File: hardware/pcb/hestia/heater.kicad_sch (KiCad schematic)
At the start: 19 parts, among them Q1 FDS8876, SW2 SW_Push_Open, U10 INA826

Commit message: changes
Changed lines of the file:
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@@
     (effects (font (size 1.27 1.27)) (justify left bottom))
   )
-  (label "Heater low" (at 135.89 103.505 0)
+  (label "Heater low" (at 136.525 103.505 0)
     (effects (font (size 1.27 1.27)) (justify left bottom))
   )

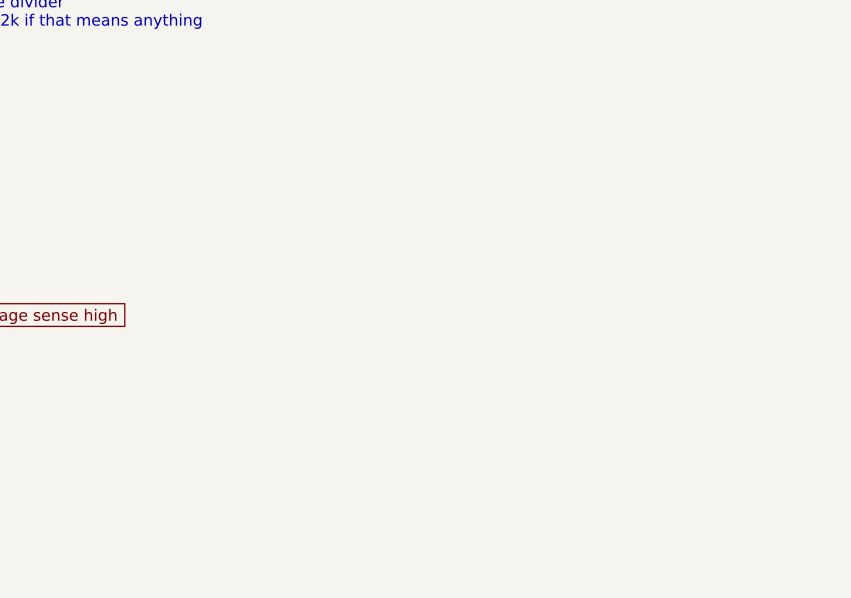
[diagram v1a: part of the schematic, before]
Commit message: pcb: lots of schematic cleanup, board not yet updated
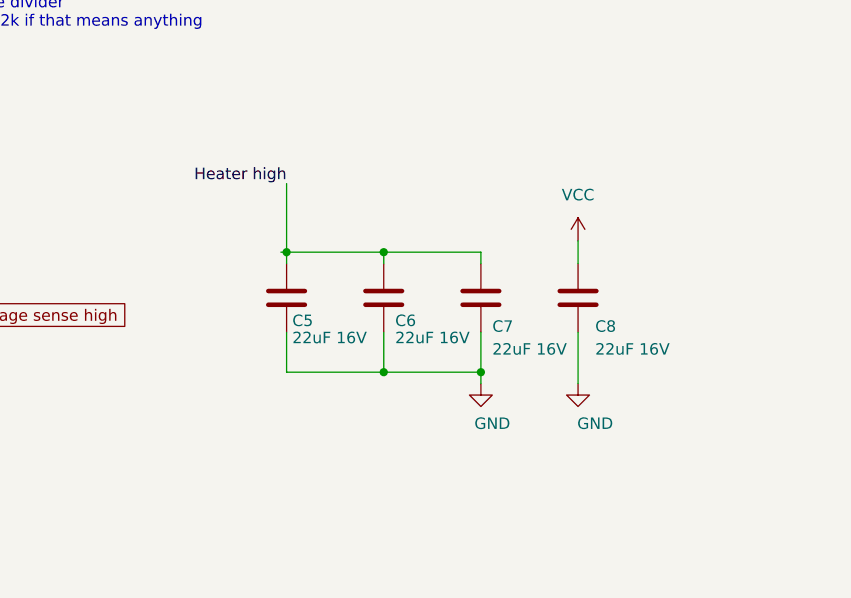
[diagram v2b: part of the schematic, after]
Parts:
- added C5, C6, C7, C8: 22uF 16V, Capacitor_SMD:C_1206_3216Metric, symbol Device:C
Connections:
- net GND: now also C5.2, C6.2, C7.2, C8.2
- net Heater high: now also C5.1, C6.1, C7.1
- net VCC: now also C8.1
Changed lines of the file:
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@@
   (junction (at 103.505 56.515) (diameter 0) (color 0 0 0 0)
   )
+  (junction (at 228.6 72.39) (diameter 0) (color 0 0 0 0)
+  )
   (junction (at 88.265 74.295) (diameter 0) (color 0 0 0 0)
   )
   (junction (at 112.395 122.555) (diameter 0) (color 0 0 0 0)
   )
+  (junction (at 217.805 59.055) (diameter 0) (color 0 0 0 0)
+  )
   (junction (at 83.185 60.96) (diameter 0) (color 0 0 0 0)
   )
+  (junction (at 217.805 72.39) (diameter 0) (color 0 0 0 0)
+  )
   (junction (at 129.54 131.445) (diameter 0) (color 0 0 0 0)
   )
@@
   (junction (at 81.915 51.435) (diameter 0) (color 0 0 0 0)
   )
+  (junction (at 207.01 59.055) (diameter 0) (color 0 0 0 0)
+  )
   (junction (at 129.54 89.535) (diameter 0) (color 0 0 0 0)
   )
+  (wire (pts (xy 207.01 72.39) (xy 217.805 72.39))
+    (stroke (width 0) (type default) (color 0 0 0 0))
+  )
   (wire (pts (xy 88.265 79.375) (xy 88.265 81.915))
     (stroke (width 0) (type default) (color 0 0 0 0))
@@
     (stroke (width 0) (type default) (color 0 0 0 0))
   )
+  (wire (pts (xy 207.01 59.055) (xy 206.375 59.055))
+    (stroke (width 0) (type default) (color 0 0 0 0))
+  )
   (wire (pts (xy 81.915 51.435) (xy 103.505 51.435))
     (stroke (width 0) (type default) (color 0 0 0 0))
@@
     (stroke (width 0) (type default) (color 0 0 0 0))
   )
+  (wire (pts (xy 207.01 67.945) (xy 207.01 72.39))
+    (stroke (width 0) (type default) (color 0 0 0 0))
+  )
   (wire (pts (xy 129.54 89.535) (xy 135.89 89.535))
     (stroke (width 0) (type default) (color 0 0 0 0))
@@
     (stroke (width 0) (type default) (color 0 0 0 0))
   )
+  (wire (pts (xy 207.01 51.435) (xy 207.01 59.055))
+    (stroke (width 0) (type default) (color 0 0 0 0))
+  )
+  (wire (pts (xy 207.01 59.055) (xy 207.01 60.325))
+    (stroke (width 0) (type default) (color 0 0 0 0))
+  )
   (wire (pts (xy 103.505 64.135) (xy 103.505 56.515))
     (stroke (width 0) (type default) (color 0 0 0 0))
@@
     (stroke (width 0) (type default) (color 0 0 0 0))
   )
+  (wire (pts (xy 228.6 59.055) (xy 228.6 60.325))
+    (stroke (width 0) (type default) (color 0 0 0 0))
+  )
   (wire (pts (xy 100.965 141.605) (xy 100.965 142.875))
     (stroke (width 0) (type default) (color 0 0 0 0))
@@
     (stroke (width 0) (type default) (color 0 0 0 0))
   )
+  (wire (pts (xy 217.805 59.055) (xy 228.6 59.055))
+    (stroke (width 0) (type default) (color 0 0 0 0))
+  )
   (wire (pts (xy 127 102.235) (xy 127 104.775))
     (stroke (width 0) (type default) (color 0 0 0 0))
@@
     (stroke (width 0) (type default) (color 0 0 0 0))
   )
+  (wire (pts (xy 239.395 57.785) (xy 239.395 60.325))
+    (stroke (width 0) (type default) (color 0 0 0 0))
+  )
   (wire (pts (xy 106.045 86.995) (xy 106.045 88.265))
     (stroke (width 0) (type default) (color 0 0 0 0))
@@
     (stroke (width 0) (type default) (color 0 0 0 0))
   )
+  (wire (pts (xy 217.805 67.945) (xy 217.805 72.39))
+    (stroke (width 0) (type default) (color 0 0 0 0))
+  )
+  (wire (pts (xy 239.395 67.945) (xy 239.395 73.66))
+    (stroke (width 0) (type default) (color 0 0 0 0))
+  )
   (wire (pts (xy 129.54 131.445) (xy 129.54 133.985))
     (stroke (width 0) (type default) (color 0 0 0 0))
   )
+  (wire (pts (xy 217.805 72.39) (xy 228.6 72.39))
+    (stroke (width 0) (type default) (color 0 0 0 0))
+  )
+  (wire (pts (xy 228.6 72.39) (xy 228.6 73.66))
+    (stroke (width 0) (type default) (color 0 0 0 0))
+  )
   (wire (pts (xy 98.425 122.555) (xy 100.965 122.555))
     (stroke (width 0) (type default) (color 0 0 0 0))
@@
     (stroke (width 0) (type default) (color 0 0 0 0))
   )
+  (wire (pts (xy 217.805 60.325) (xy 217.805 59.055))
+    (stroke (width 0) (type default) (color 0 0 0 0))
+  )
   (wire (pts (xy 103.505 56.515) (xy 103.505 51.435))
     (stroke (width 0) (type default) (color 0 0 0 0))
@@
     (stroke (width 0) (type default) (color 0 0 0 0))
   )
+  (wire (pts (xy 207.01 59.055) (xy 217.805 59.055))
+    (stroke (width 0) (type default) (color 0 0 0 0))
+  )
   (wire (pts (xy 118.745 59.055) (xy 118.745 61.595))
     (stroke (width 0) (type default) (color 0 0 0 0))
   )
   (wire (pts (xy 129.54 99.06) (xy 129.54 103.505))
+    (stroke (width 0) (type default) (color 0 0 0 0))
+  )
+  (wire (pts (xy 228.6 67.945) (xy 228.6 72.39))
     (stroke (width 0) (type default) (color 0 0 0 0))
   )
@@
     (at 158.115 34.29 0)
     (effects (font (size 1.27 1.27)) (justify left bottom))
+  )
+  (label "Heater high" (at 207.01 51.435 180)
+    (effects (font (size 1.27 1.27)) (justify right bottom))
   )
   (label "Heater high" (at 163.83 54.61 90)
@@
     (pin "1")
   )
+  (symbol (lib_id "power:VCC") (at 239.395 57.785 0) (unit 1)
+    (in_bom yes) (on_board yes) (fields_autoplaced)
+    (property "Reference" "#PWR07" (id 0) (at 239.395 61.595 0)
+      (effects (font (size 1.27 1.27)) hide)
+    )
+    (property "Value" "VCC" (id 1) (at 239.395 52.705 0))
+    (property "Footprint" "" (id 2) (at 239.395 57.785 0)
+      (effects (font (size 1.27 1.27)) hide)
+    )
+    (property "Datasheet" "" (id 3) (at 239.395 57.785 0)
+      (effects (font (size 1.27 1.27)) hide)
+    )
+    (pin "1")
+  )
   (symbol (lib_id "power:VCC") (at 129.54 73.66 0) (unit 1)
     (in_bom yes) (on_board yes) (fields_autoplaced)
@@
     )
     (pin "1")
+  )
+  (symbol (lib_id "Device:C") (at 239.395 64.135 0) (unit 1)
+    (in_bom yes) (on_board yes)
+    (property "Reference" "C8" (id 0) (at 241.3 67.31 0)
+      (effects (font (size 1.27 1.27)) (justify left))
+    )
+    (property "Value" "22uF 16V" (id 1) (at 241.3 69.85 0)
+      (effects (font (size 1.27 1.27)) (justify left))
+    )
+    (property "Footprint" "Capacitor_SMD:C_1206_3216Metric" (id 2) (at 240.3602 67.945 0)
+      (effects (font (size 1.27 1.27)) hide)
+    )
+    (property "Datasheet" "~" (id 3) (at 239.395 64.135 0)
+      (effects (font (size 1.27 1.27)) hide)
+    )
+    (property "LCSC Part" "C13585" (id 4) (at 239.395 64.135 0)
+      (effects (font (size 1.27 1.27)) hide)
+    )
+    (pin "1")
+    (pin "2")
   )
   (symbol (lib_id "Device:R") (at 106.045 122.555 90) (unit 1)
@@
     (pin "2")
   )
+  (symbol (lib_id "power:GND") (at 228.6 73.66 0) (unit 1)
+    (in_bom yes) (on_board yes)
+    (property "Reference" "#PWR0173" (id 0) (at 228.6 80.01 0)
+      (effects (font (size 1.27 1.27)) hide)
+    )
+    (property "Value" "GND" (id 1) (at 229.87 78.105 0))
+    (property "Footprint" "" (id 2) (at 228.6 73.66 0)
+      (effects (font (size 1.27 1.27)) hide)
+    )
+    (property "Datasheet" "" (id 3) (at 228.6 73.66 0)
+      (effects (font (size 1.27 1.27)) hide)
+    )
+    (pin "1")
+  )
   (symbol (lib_id "Device:R") (at 163.195 103.505 180) (unit 1)
     (in_bom yes) (on_board yes) (fields_autoplaced)
@@
     (pin "2")
   )
+  (symbol (lib_id "Device:C") (at 217.805 64.135 0) (unit 1)
+    (in_bom yes) (on_board yes)
+    (property "Reference" "C6" (id 0) (at 219.075 66.675 0)
+      (effects (font (size 1.27 1.27)) (justify left))
+    )
+    (property "Value" "22uF 16V" (id 1) (at 219.075 68.58 0)
+      (effects (font (size 1.27 1.27)) (justify left))
+    )
+    (property "Footprint" "Capacitor_SMD:C_1206_3216Metric" (id 2) (at 218.7702 67.945 0)
+      (effects (font (size 1.27 1.27)) hide)
+    )
+    (property "Datasheet" "~" (id 3) (at 217.805 64.135 0)
+      (effects (font (size 1.27 1.27)) hide)
+    )
+    (property "LCSC Part" "C13585" (id 4) (at 217.805 64.135 0)
+      (effects (font (size 1.27 1.27)) hide)
+    )
+    (pin "1")
+    (pin "2")
+  )
   (symbol (lib_id "Device:R") (at 100.965 130.175 0) (unit 1)
     (in_bom yes) (on_board yes)
@@
     (pin "2")
   )
+  (symbol (lib_id "Device:C") (at 207.01 64.135 0) (unit 1)
+    (in_bom yes) (on_board yes)
+    (property "Reference" "C5" (id 0) (at 207.645 66.675 0)
+      (effects (font (size 1.27 1.27)) (justify left))
+    )
+    (property "Value" "22uF 16V" (id 1) (at 207.645 68.58 0)
+      (effects (font (size 1.27 1.27)) (justify left))
+    )
+    (property "Footprint" "Capacitor_SMD:C_1206_3216Metric" (id 2) (at 207.9752 67.945 0)
+      (effects (font (size 1.27 1.27)) hide)
+    )
+    (property "Datasheet" "~" (id 3) (at 207.01 64.135 0)
+      (effects (font (size 1.27 1.27)) hide)
+    )
+    (property "LCSC Part" "C13585" (id 4) (at 207.01 64.135 0)
+      (effects (font (size 1.27 1.27)) hide)
+    )
+    (pin "1")
+    (pin "2")
+  )
   (symbol (lib_id "power:VCC") (at 118.745 48.895 0) (unit 1)
     (in_bom yes) (on_board yes)
@@
     )
     (pin "1")
+  )
+  (symbol (lib_id "Device:C") (at 228.6 64.135 0) (unit 1)
+    (in_bom yes) (on_board yes)
+    (property "Reference" "C7" (id 0) (at 229.87 67.31 0)
+      (effects (font (size 1.27 1.27)) (justify left))
+    )
+    (property "Value" "22uF 16V" (id 1) (at 229.87 69.85 0)
+      (effects (font (size 1.27 1.27)) (justify left))
+    )
+    (property "Footprint" "Capacitor_SMD:C_1206_3216Metric" (id 2) (at 229.5652 67.945 0)
+      (effects (font (size 1.27 1.27)) hide)
+    )
+    (property "Datasheet" "~" (id 3) (at 228.6 64.135 0)
+      (effects (font (size 1.27 1.27)) hide)
+    )
+    (property "LCSC Part" "C13585" (id 4) (at 228.6 64.135 0)
+      (effects (font (size 1.27 1.27)) hide)
+    )
+    (pin "1")
+    (pin "2")
   )
   (symbol (lib_id "Transistor_FET:FDS6630A") (at 127 122.555 0) (unit 1)
@@
     (pin "2")
   )
+  (symbol (lib_id "power:GND") (at 239.395 73.66 0) (unit 1)
+    (in_bom yes) (on_board yes)
+    (property "Reference" "#PWR08" (id 0) (at 239.395 80.01 0)
+      (effects (font (size 1.27 1.27)) hide)
+    )
+    (property "Value" "GND" (id 1) (at 241.3 78.105 0))
+    (property "Footprint" "" (id 2) (at 239.395 73.66 0)
+      (effects (font (size 1.27 1.27)) hide)
+    )
+    (property "Datasheet" "" (id 3) (at 239.395 73.66 0)
+      (effects (font (size 1.27 1.27)) hide)
+    )
+    (pin "1")
+  )
 )

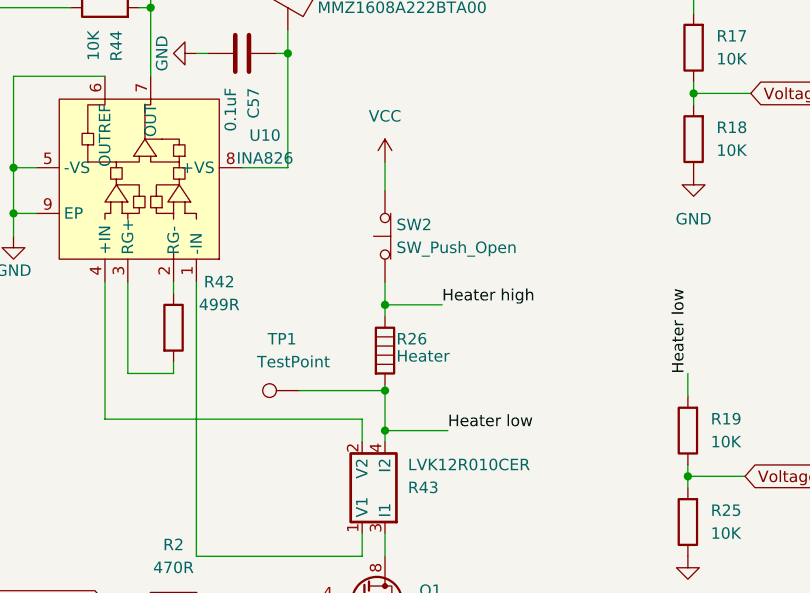
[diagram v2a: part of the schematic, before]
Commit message: pcb: more cleanup on heater schematic
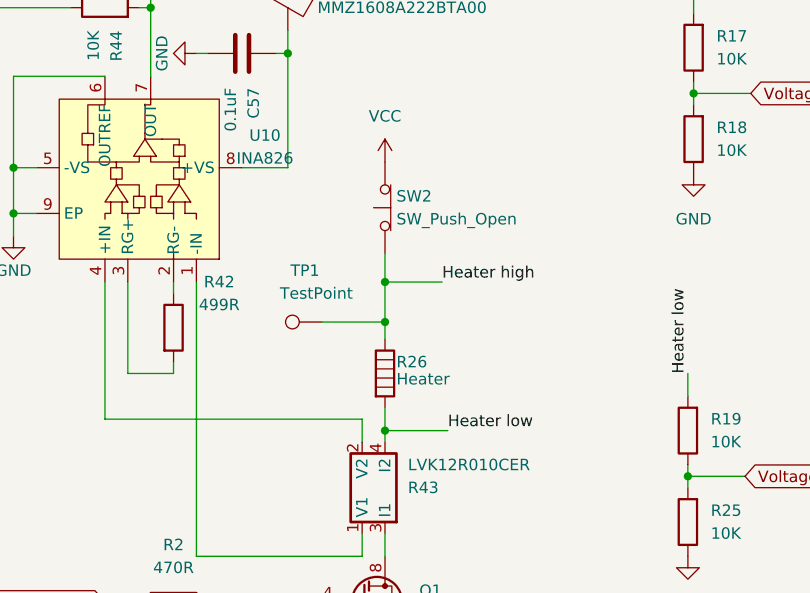
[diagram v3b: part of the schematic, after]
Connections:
- net Heater high: now also TP1.1
- net Heater low: no longer TP1.1
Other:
- moved on the sheet: R26, SW2, TP1
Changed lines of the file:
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@@
 (kicad_sch (version 20211123) (generator eeschema)
   (paper "A4")
-  (junction (at 129.54 99.06) (diameter 0) (color 0 0 0 0)
-  )
   (junction (at 103.505 56.515) (diameter 0) (color 0 0 0 0)
   )
+  (junction (at 129.54 91.44) (diameter 0) (color 0 0 0 0)
+  )
   (junction (at 228.6 72.39) (diameter 0) (color 0 0 0 0)
   )
@@
   (junction (at 207.01 59.055) (diameter 0) (color 0 0 0 0)
   )
-  (junction (at 129.54 89.535) (diameter 0) (color 0 0 0 0)
+  (junction (at 129.54 86.995) (diameter 0) (color 0 0 0 0)
   )
   (wire (pts (xy 207.01 72.39) (xy 217.805 72.39))
@@
     (stroke (width 0) (type default) (color 0 0 0 0))
   )
-  (wire (pts (xy 120.015 99.06) (xy 129.54 99.06))
-    (stroke (width 0) (type default) (color 0 0 0 0))
-  )
-  (wire (pts (xy 129.54 98.425) (xy 129.54 99.06))
+  (wire (pts (xy 129.54 83.82) (xy 129.54 86.995))
+    (stroke (width 0) (type default) (color 0 0 0 0))
+  )
+  (wire (pts (xy 129.54 100.965) (xy 129.54 103.505))
     (stroke (width 0) (type default) (color 0 0 0 0))
   )
@@
     (stroke (width 0) (type default) (color 0 0 0 0))
   )
-  (wire (pts (xy 129.54 73.66) (xy 129.54 76.835))
-    (stroke (width 0) (type default) (color 0 0 0 0))
-  )
   (wire (pts (xy 163.83 66.04) (xy 170.18 66.04))
     (stroke (width 0) (type default) (color 0 0 0 0))
@@
     (stroke (width 0) (type default) (color 0 0 0 0))
   )
+  (wire (pts (xy 122.555 91.44) (xy 129.54 91.44))
+    (stroke (width 0) (type default) (color 0 0 0 0))
+  )
   (wire (pts (xy 109.855 122.555) (xy 112.395 122.555))
     (stroke (width 0) (type default) (color 0 0 0 0))
@@
     (stroke (width 0) (type default) (color 0 0 0 0))
   )
-  (wire (pts (xy 129.54 89.535) (xy 135.89 89.535))
+  (wire (pts (xy 129.54 86.995) (xy 135.89 86.995))
     (stroke (width 0) (type default) (color 0 0 0 0))
   )
@@
     (stroke (width 0) (type default) (color 0 0 0 0))
   )
-  (wire (pts (xy 129.54 89.535) (xy 129.54 90.805))
+  (wire (pts (xy 129.54 86.995) (xy 129.54 91.44))
     (stroke (width 0) (type default) (color 0 0 0 0))
   )
@@
     (stroke (width 0) (type default) (color 0 0 0 0))
   )
+  (wire (pts (xy 129.54 91.44) (xy 129.54 93.345))
+    (stroke (width 0) (type default) (color 0 0 0 0))
+  )
   (wire (pts (xy 100.965 122.555) (xy 100.965 126.365))
     (stroke (width 0) (type default) (color 0 0 0 0))
@@
     (stroke (width 0) (type default) (color 0 0 0 0))
   )
-  (wire (pts (xy 129.54 99.06) (xy 129.54 103.505))
-    (stroke (width 0) (type default) (color 0 0 0 0))
-  )
   (wire (pts (xy 228.6 67.945) (xy 228.6 72.39))
     (stroke (width 0) (type default) (color 0 0 0 0))
   )
   (wire (pts (xy 163.83 66.04) (xy 163.83 67.31))
-    (stroke (width 0) (type default) (color 0 0 0 0))
-  )
-  (wire (pts (xy 129.54 86.995) (xy 129.54 89.535))
     (stroke (width 0) (type default) (color 0 0 0 0))
   )
@@
     (effects (font (size 1.27 1.27)) (justify left bottom))
   )
-  (label "Heater high" (at 135.89 89.535 0)
+  (label "Heater high" (at 135.89 86.995 0)
     (effects (font (size 1.27 1.27)) (justify left bottom))
   )
@@
     )
   )
-  (symbol (lib_id "Device:Heater") (at 129.54 94.615 0) (unit 1)
-    (in_bom yes) (on_board yes)
-    (property "Reference" "R26" (id 0) (at 130.81 93.345 0)
-      (effects (font (size 1.27 1.27)) (justify left))
-    )
-    (property "Value" "Heater" (id 1) (at 130.81 95.25 0)
-      (effects (font (size 1.27 1.27)) (justify left))
-    )
-    (property "Footprint" "" (id 2) (at 127.762 94.615 90)
-      (effects (font (size 1.27 1.27)) hide)
-    )
-    (property "Datasheet" "~" (id 3) (at 129.54 94.615 0)
+  (symbol (lib_id "Device:Heater") (at 129.54 97.155 0) (unit 1)
+    (in_bom yes) (on_board yes)
+    (property "Reference" "R26" (id 0) (at 130.81 95.885 0)
+      (effects (font (size 1.27 1.27)) (justify left))
+    )
+    (property "Value" "Heater" (id 1) (at 130.81 97.79 0)
+      (effects (font (size 1.27 1.27)) (justify left))
+    )
+    (property "Footprint" "" (id 2) (at 127.762 97.155 90)
+      (effects (font (size 1.27 1.27)) hide)
+    )
+    (property "Datasheet" "~" (id 3) (at 129.54 97.155 0)
       (effects (font (size 1.27 1.27)) hide)
     )
@@
     (pin "1")
   )
-  (symbol (lib_id "Switch:SW_Push_Open") (at 129.54 81.915 90) (unit 1)
-    (in_bom yes) (on_board yes) (fields_autoplaced)
-    (property "Reference" "SW2" (id 0) (at 130.81 80.6449 90)
-      (effects (font (size 1.27 1.27)) (justify right))
-    )
-    (property "Value" "SW_Push_Open" (id 1) (at 130.81 83.1849 90)
-      (effects (font (size 1.27 1.27)) (justify right))
-    )
-    (property "Footprint" "Connector_PinHeader_2.54mm:PinHeader_1x02_P2.54mm_Vertical" (id 2) (at 124.46 81.915 0)
-      (effects (font (size 1.27 1.27)) hide)
-    )
-    (property "Datasheet" "~" (id 3) (at 124.46 81.915 0)
+  (symbol (lib_id "Switch:SW_Push_Open") (at 129.54 78.74 90) (unit 1)
+    (in_bom yes) (on_board yes) (fields_autoplaced)
+    (property "Reference" "SW2" (id 0) (at 130.81 77.4699 90)
+      (effects (font (size 1.27 1.27)) (justify right))
+    )
+    (property "Value" "SW_Push_Open" (id 1) (at 130.81 80.0099 90)
+      (effects (font (size 1.27 1.27)) (justify right))
+    )
+    (property "Footprint" "Connector_PinHeader_2.54mm:PinHeader_1x02_P2.54mm_Vertical" (id 2) (at 124.46 78.74 0)
+      (effects (font (size 1.27 1.27)) hide)
+    )
+    (property "Datasheet" "~" (id 3) (at 124.46 78.74 0)
       (effects (font (size 1.27 1.27)) hide)
     )
@@
     (pin "2")
   )
-  (symbol (lib_id "Connector:TestPoint") (at 120.015 99.06 90) (unit 1)
-    (in_bom yes) (on_board yes)
-    (property "Reference" "TP1" (id 0) (at 118.11 93.345 90))
-    (property "Value" "TestPoint" (id 1) (at 119.38 95.885 90))
-    (property "Footprint" "TestPoint:TestPoint_Pad_2.0x2.0mm" (id 2) (at 120.015 93.98 0)
-      (effects (font (size 1.27 1.27)) hide)
-    )
-    (property "Datasheet" "~" (id 3) (at 120.015 93.98 0)
-      (effects (font (size 1.27 1.27)) hide)
-    )
+  (symbol (lib_id "Connector:TestPoint") (at 122.555 91.44 90) (unit 1)
+    (in_bom yes) (on_board yes)
+    (property "Reference" "TP1" (id 0) (at 120.65 85.725 90))
+    (property "Value" "TestPoint" (id 1) (at 121.92 88.265 90))
+    (property "Footprint" "TestPoint:TestPoint_Pad_2.0x2.0mm" (id 2) (at 122.555 86.36 0)
+      (effects (font (size 1.27 1.27)) hide)
+    )
+    (property "Datasheet" "~" (id 3) (at 122.555 86.36 0)
+      (effects (font (size 1.27 1.27)) hide)
+    )

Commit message: pcb: add heater net-tie to resolve net problems, move voltage divider out from under heater, fixed traces going into H2 courtyard, restored D1 LED designator, silkscreen updates. Didn't get Pico-Lock mounting pads fixed yet.
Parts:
- R26: footprint (none) -> NetTie:NetTie-2_SMD_Pad0.5mm; now left out of the parts list
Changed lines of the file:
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@@
   )
   (symbol (lib_id "Device:Heater") (at 129.54 97.155 0) (unit 1)
-    (in_bom yes) (on_board yes)
+    (in_bom no) (on_board yes)
     (property "Reference" "R26" (id 0) (at 130.81 95.885 0)
       (effects (font (size 1.27 1.27)) (justify left))
@@
       (effects (font (size 1.27 1.27)) (justify left))
     )
-    (property "Footprint" "" (id 2) (at 127.762 97.155 90)
+    (property "Footprint" "NetTie:NetTie-2_SMD_Pad0.5mm" (id 2) (at 127.762 97.155 90)
       (effects (font (size 1.27 1.27)) hide)
     )
